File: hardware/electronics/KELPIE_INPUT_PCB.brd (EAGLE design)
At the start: 101.6 x 57.1 mm, 27 parts, among them J1 30_PIN_CONNECTOR_MALEFLEX_CON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

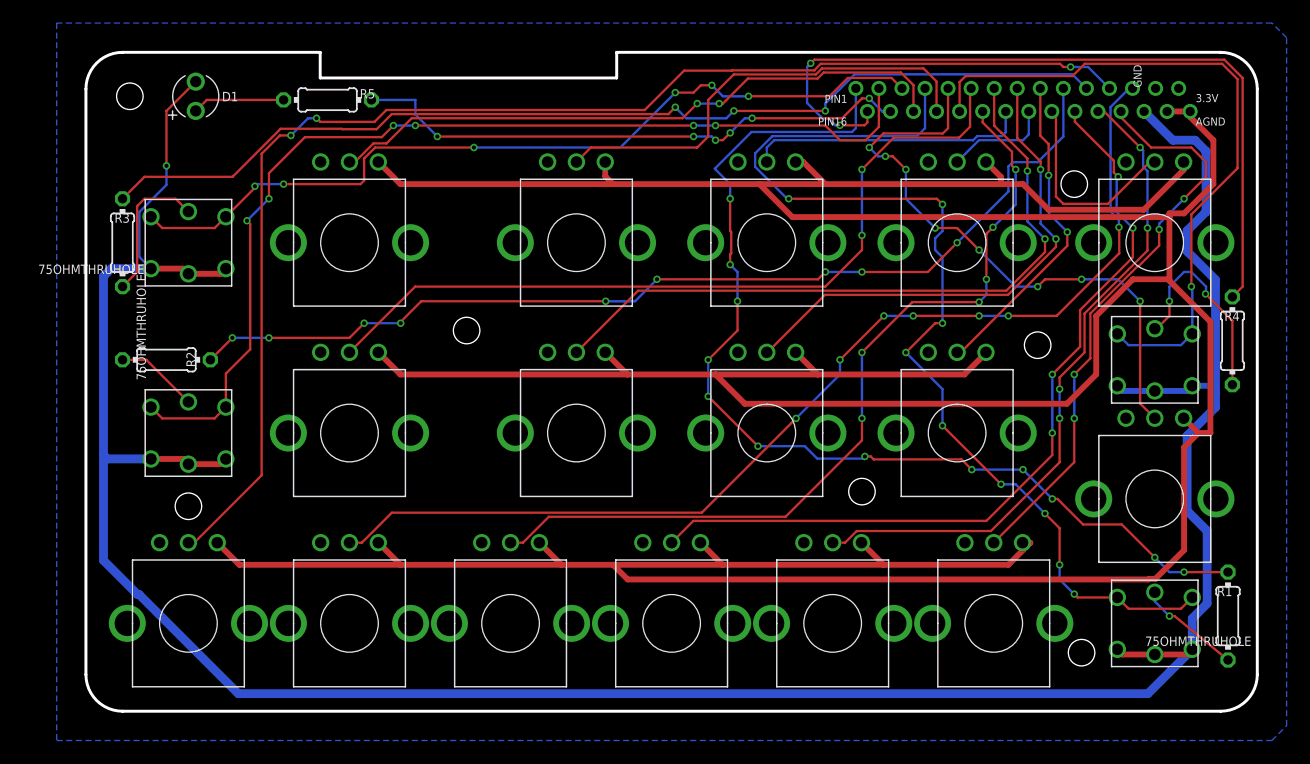
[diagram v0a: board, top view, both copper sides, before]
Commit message: board rev 2 done, sent to seeed for manufacture
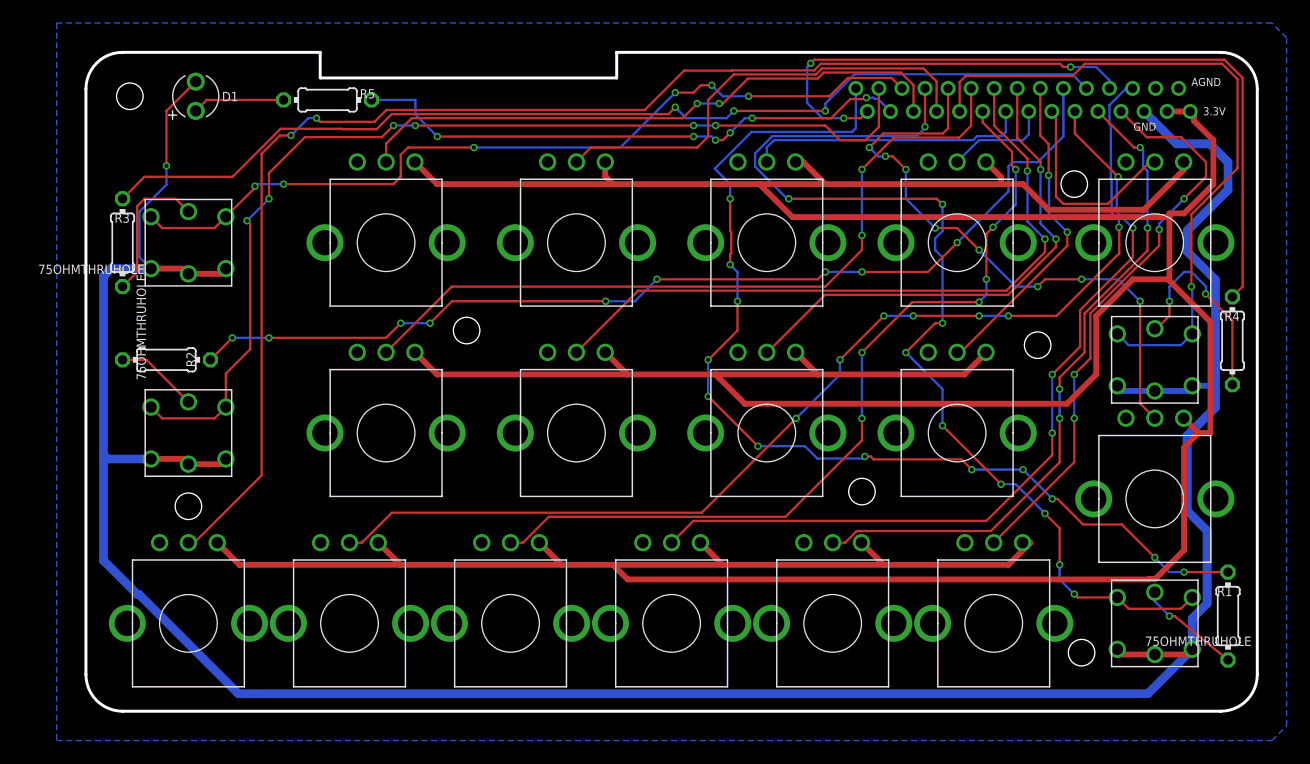
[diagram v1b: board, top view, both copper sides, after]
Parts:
- J1: value 30_PIN_CONNECTOR_MALEFLEX_CONNECTOR -> 30_PIN_CONNECTOR_MALE; device sirin-clone-library:SLW30S -> sirin-clone-library:SLW30S_BOTTOM
- moved U$14 3.18 mm to (26.0, 24.1)
- moved U$8 3.18 mm to (26.0, 40.6)
- flipped J1 to the top, turned to 0 degrees
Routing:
- net 3.3V: track 409.0 -> 402.6 mm
- net PIN29/KNOB9: track 69.4 -> 66.2 mm
- net PIN20/KNOB4: track 54.9 -> 52.6 mm
- net GND: track 236.5 -> 238.6 mm
- net PIN33/LED4: track 68.3 -> 67.2 mm
- net PIN2/SW1: vias 9 -> 10
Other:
- board text added: "CONTROL BOARD V0.1.0 AUGUST 2019 BY K. MARUT"
- board text removed: "CONTROL BOARD V0.0.1 MAR 2019 BY K. MARUT"
- board text removed: "PIN1"
- board text removed: "PIN16"
